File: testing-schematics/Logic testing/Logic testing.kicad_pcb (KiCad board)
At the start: 2 copper layers, 79 x 76.8 mm, 47 parts, among them IC1 ESP32-C6-WROOM-1U-N8, J1 External Box, J2 Aux Wire, J3 Conn_01x04, J4 Lame Tab, J5 Test Output, K1 G6K-2, K2 G6K-2, K3 G6K-2, K4 G6K-2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

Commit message: Work from 14th
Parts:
- added J6: Small Pin, Connector_Wire:SolderWire-0.5sqmm_1x01_D0.9mm_OD2.1mm, F.Cu at (117.2, 106.8)
- SW3: footprint Button_Switch_THT:SW_PUSH-12mm -> Button_Switch_THT:SW_PUSH_6mm_H13mm
- moved SW3 99.1 mm to (136.5, 111.8), turned to 180 degrees
- moved R9 66.4 mm to (91.5, 60.5)
- moved R11 53.3 mm to (124.0, 53.5), turned to 90 degrees
- moved C3 52.3 mm to (128.2, 53.5), turned to 90 degrees
- moved R5 52.1 mm to (94.2, 92.1)
- moved R7 50.3 mm to (94.2, 97.0)
- moved R4 48.2 mm to (94.2, 87.2), turned to 180 degrees
- moved R6 41.8 mm to (103.5, 94.4)
- moved R3 40.5 mm to (103.5, 90.6), turned to 180 degrees
- moved R2 39.3 mm to (103.5, 86.8), turned to 180 degrees
- moved R12 32.2 mm to (110.2, 90.6)
- moved R1 31.4 mm to (103.5, 98.2)
- moved R15 30.7 mm to (110.2, 86.8)
- moved R14 23.6 mm to (110.2, 94.4)
- moved R13 17.8 mm to (110.2, 98.2)
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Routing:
- net Net-(D4-A): track 0.00 -> 95.5 mm, vias 0 -> 3
- net Net-(D3-A): track 0.00 -> 80.5 mm
- net SG1: track 0.00 -> 66.6 mm, vias 0 -> 2
- net BTN USE: track 0.00 -> 63.7 mm, vias 0 -> 2
- net LAME: track 0.00 -> 57.2 mm, vias 0 -> 2
- net Net-(D1-A): track 0.00 -> 52.7 mm
- net Net-(P1-SHIELD): track 0.00 -> 52.3 mm, vias 0 -> 1
- net B2: track 0.00 -> 50.9 mm
- net VDR3: track 0.00 -> 50.0 mm, vias 0 -> 2
- net A1: track 0.00 -> 47.4 mm
- net Net-(Q1-B): track 0.00 -> 46.7 mm
- net Net-(Q2-B): track 0.00 -> 46.1 mm, vias 0 -> 1
- net Net-(D2-A): track 0.00 -> 44.5 mm
- net Net-(SW1-C): track 0.00 -> 40.9 mm, vias 0 -> 2
- net B1: track 0.00 -> 38.6 mm
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- added copper zone on B.Cu, net VD1
- added copper zone on F.Cu, net VD1
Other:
- board size 79 x 76.8 mm -> 79 x 78.2 mm

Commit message: Finished PCB
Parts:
- moved SW2 0.16 mm to (100.8, 49.6)
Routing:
- net WT2: track 27.8 -> 182.0 mm, vias 0 -> 9
- net +5V: track 27.4 -> 175.1 mm, vias 2 -> 8
- net C1: track 15.5 -> 79.7 mm, vias 0 -> 4
- net C2: track 15.5 -> 77.2 mm, vias 0 -> 3
- net A2: track 36.4 -> 93.1 mm, vias 0 -> 2
- net Net-(Q4-B): track 0.00 -> 48.6 mm, vias 0 -> 3
- net VDR2: track 20.7 -> 58.9 mm, vias 0 -> 2
- net WT1: track 0.00 -> 36.6 mm, vias 0 -> 2
- net WPS A: track 28.6 -> 59.3 mm, vias 2 -> 4
- net WPS B: track 26.6 -> 56.9 mm, vias 2 -> 3
- net VDR1: track 29.9 -> 54.1 mm, vias 0 -> 2
- net WT3: track 0.00 -> 20.7 mm, vias 0 -> 2
- net VD1: track 18.1 -> 31.0 mm, vias 2 -> 38
- net Net-(JP1-A): track 0.00 -> 9.68 mm
- net Net-(P1-SHIELD): track 52.3 -> 58.2 mm, vias 1 -> 0
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
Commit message: Finished PCB; Updated USB-C connector; Stated on CAD
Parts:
- added H5: MountingHole, MountingHole:MountingHole_2.2mm_M2_DIN965_Pad_TopBottom, F.Cu at (115.2, 58.8)
- added H6: MountingHole, MountingHole:MountingHole_2.2mm_M2_DIN965_Pad_TopBottom, F.Cu at (86.2, 58.8)
- added H7: MountingHole, MountingHole:MountingHole_2.2mm_M2_DIN965_Pad_TopBottom, F.Cu at (115.2, 100.8)
- added H8: MountingHole, MountingHole:MountingHole_2.2mm_M2_DIN965_Pad_TopBottom, F.Cu at (86.2, 100.8)
- P1: footprint Connector_USB:USB_C_Receptacle_GCT_USB4105-xx-A_16P_TopMnt_Horizontal -> Connector_USB:USB_C_Receptacle_GCT_USB4085
- moved P1 3.57 mm to (91.9, 53.4)
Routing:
- net VD1: track 31.0 -> 19.3 mm, vias 38 -> 40
- net Net-(P1-SHIELD): track 58.2 -> 53.2 mm, vias 0 -> 1
- net +5V: track 175.1 -> 178.7 mm, vias 8 -> 7
- net USB_D-: track 27.4 -> 30.6 mm, vias 2 -> 1
- net USB_D+: track 28.5 -> 30.9 mm, vias 2 -> 1
- net Net-(P1-CC): track 6.20 -> 8.10 mm
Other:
- outline, holes or cut-outs redrawn
- board text added: "FencingTester V1.0.0"
- board text added: "JLCJLCJLCJLC"
- board text added: "JoshLambda | Highway 2025"

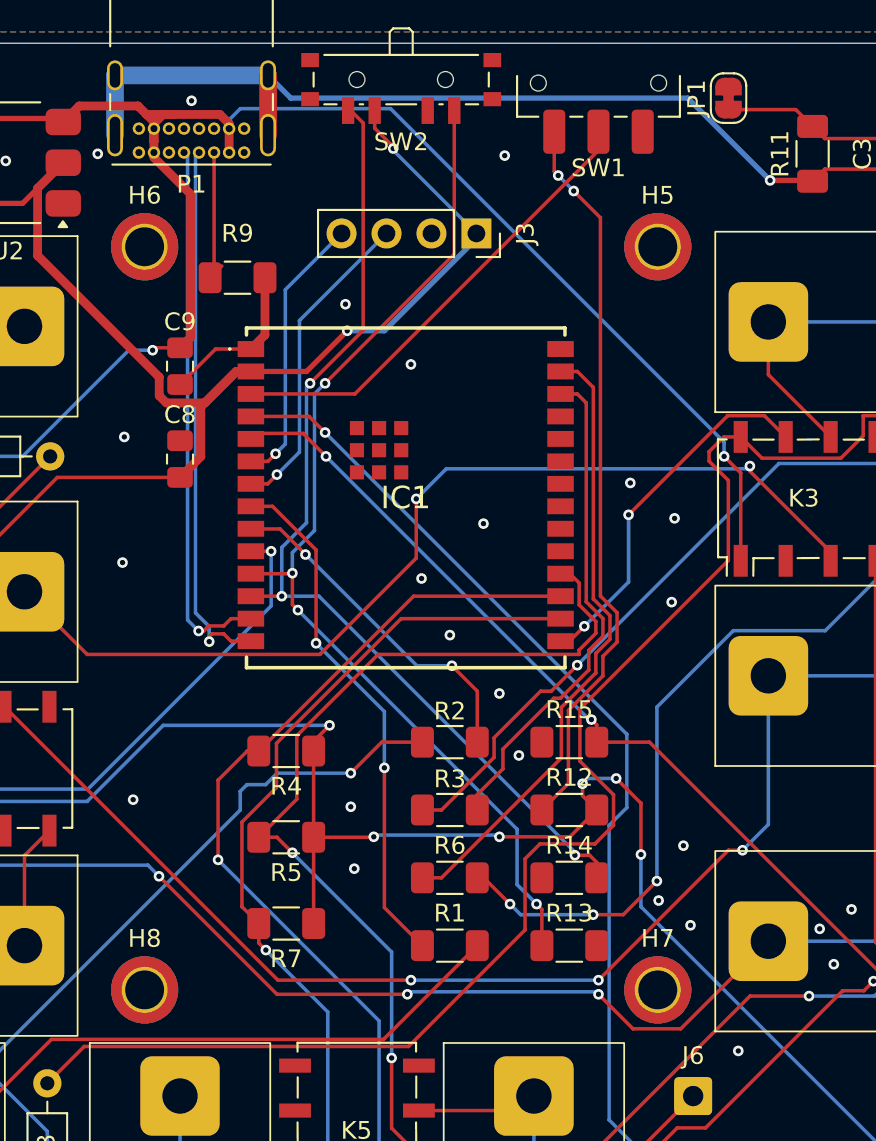
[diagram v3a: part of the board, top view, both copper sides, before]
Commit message: More final changes to PCB; Added cut outs & 3mm to CAD; Started programming
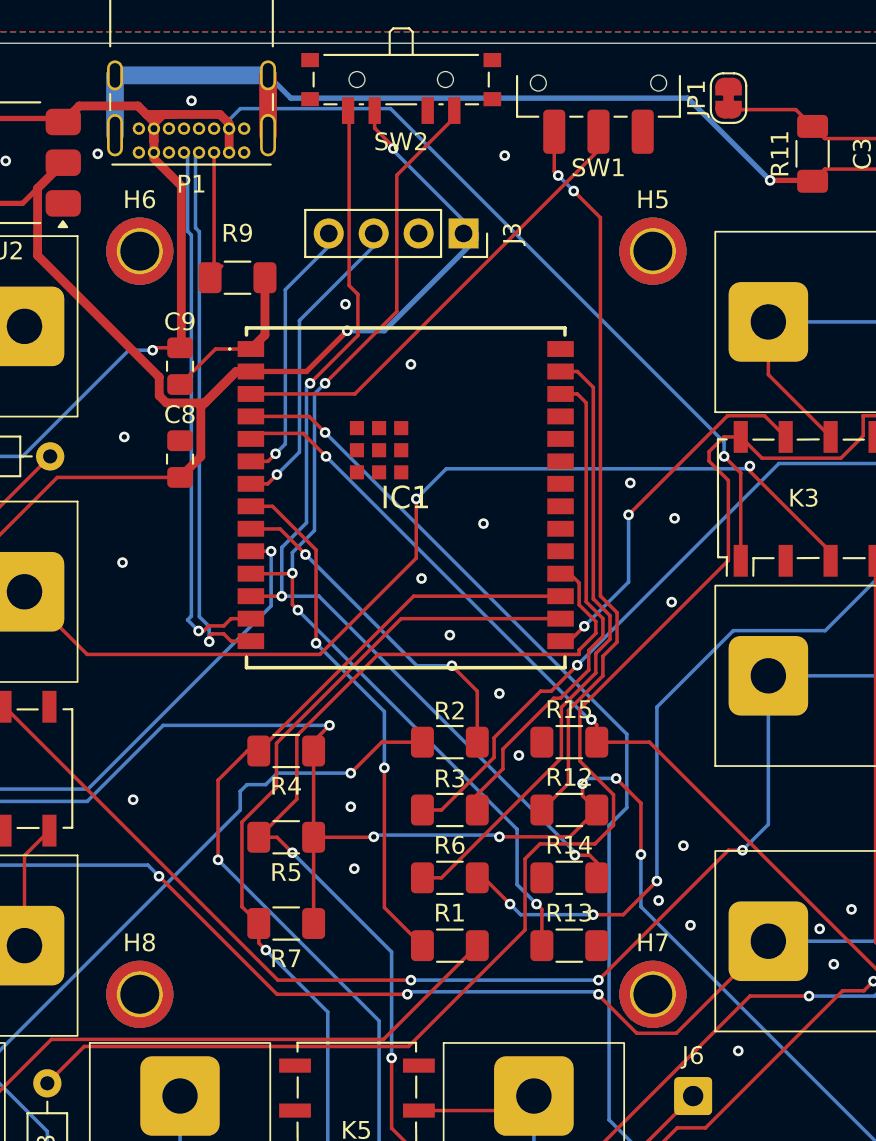
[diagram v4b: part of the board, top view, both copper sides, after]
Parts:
- moved J3 0.72 mm to (104.3, 58.0)
- moved H5 0.37 mm to (115.0, 59.0)
- moved H6 0.37 mm to (86.0, 59.0)
- moved H7 0.37 mm to (115.0, 101.0)
- moved H8 0.37 mm to (86.0, 101.0)

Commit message: Worked on  issues
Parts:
- added D5: 1N4148, Diode_SMD:D_SOD-123, F.Cu at (127.0, 89.4)
- added K6: G6K-2, Relay_SMD:Relay_DPDT_Omron_G6K-2F, F.Cu at (134.5, 73.0)
- added Q5: BC547, Package_TO_SOT_THT:TO-92_Inline, F.Cu at (123.0, 90.1)
- added R16: 10k, Custom:R_1206_3216Metric_Pad1.30x1.75mm_HandSolder_Text, F.Cu at (115.2, 73.1)
- added R17: 10k, Custom:R_1206_3216Metric_Pad1.30x1.75mm_HandSolder_Text, F.Cu at (85.3, 88.4)
- added R8: 510, Custom:R_1206_3216Metric_Pad1.30x1.75mm_HandSolder_Text, F.Cu at (116.2, 86.9)
- C3: footprint Capacitor_SMD:C_0603_1608Metric_Pad1.08x0.95mm_HandSolder -> Capacitor_SMD:C_0805_2012Metric_Pad1.18x1.45mm_HandSolder
- D1, D2, D3, D4: footprint Diode_THT:D_DO-35_SOD27_P7.62mm_Horizontal -> Diode_SMD:D_SOD-123
- R1, R11, R12, R13, R14, R15, R2, R3, R4, R5, R6, R7, R9: footprint Resistor_SMD:R_1206_3216Metric_Pad1.30x1.75mm_HandSolder -> Custom:R_1206_3216Metric_Pad1.30x1.75mm_HandSolder_Text
- moved Q4 76.2 mm to (80.3, 121.2)
- moved D3 55.7 mm to (131.8, 91.6), turned to 0 degrees
- moved Q1 43.4 mm to (78.2, 71.1), turned to 0 degrees
- moved Q2 37.5 mm to (65.2, 70.4), turned to 180 degrees
- moved R12 36.8 mm to (121.0, 55.4)
- moved R1 27.6 mm to (87.2, 76.0), turned to -90 degrees
- moved R6 27.3 mm to (80.8, 109.5), turned to -90 degrees
- moved R2 22.1 mm to (84.2, 76.0), turned to -90 degrees
- moved Q3 21.5 mm to (135.7, 90.9), turned to 0 degrees
- moved R5 19.1 mm to (112.7, 86.9), turned to 90 degrees
- moved R7 17.1 mm to (108.0, 86.9), turned to 90 degrees
- moved R4 16.1 mm to (110.3, 86.9), turned to 90 degrees
- moved R13 14.5 mm to (101.2, 86.9), turned to -90 degrees
- moved R14 13.6 mm to (99.0, 86.9), turned to 90 degrees
- moved R3 11.4 mm to (114.5, 93.2), turned to 0 degrees
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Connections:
- IC1 pad 10: WT1 -> VD1
- IC1 pad 15: WT3 -> VD1
- K4 pad 4: SG1 -> Net-(K4-Pad4)
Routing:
- net Net-(D4-A): track 95.5 -> 28.1 mm, vias 3 -> 0
- net Net-(K4-Pad4): track 0.00 -> 67.4 mm, vias 0 -> 2
- net SG1: track 66.6 -> 11.7 mm, vias 2 -> 0
- net +5V: track 178.3 -> 232.7 mm, vias 7 -> 9
- net Net-(D3-A): track 82.7 -> 30.9 mm, vias 0 -> 2
- net Net-(Q1-B): track 46.7 -> 10.8 mm
- net Net-(Q4-B): track 48.6 -> 12.8 mm, vias 3 -> 0
- net Net-(SW1-C): track 41.6 -> 12.8 mm, vias 2 -> 0
- net Net-(D1-A): track 52.7 -> 26.5 mm, vias 0 -> 1
- net Net-(D5-A): track 0.00 -> 24.8 mm
- net Net-(D2-A): track 44.5 -> 20.3 mm, vias 0 -> 1
- net REL1: track 29.6 -> 5.43 mm, vias 2 -> 0
- net Net-(Q2-B): track 46.7 -> 23.6 mm, vias 1 -> 0
- net REL4: track 35.4 -> 56.3 mm, vias 0 -> 2
- net WPS B: track 56.5 -> 40.4 mm, vias 3 -> 2
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
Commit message: Worked on PCB; worked on Code; Worked on journal
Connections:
- IC1 pad 19: unconnected-(IC1-IO21-Pad19) -> REL5
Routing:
- net REL5: track 0.00 -> 12.6 mm, vias 0 -> 2
- net VD1: vias 33 -> 57
- net C1: vias 4 -> 3
- net (no net): vias 0 -> 1
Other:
- board text added: "A1"
- board text added: "A2"
- board text added: "A3"
- board text added: "B1"
- board text added: "B2"
- board text added: "B3"
- board text added: "C1"
- board text added: "C2"
- board text added: "C3"
- board text added: "LAME"
- board text added: "OLED"
- board text added: "PWR"
- board text added: "WEAPON"

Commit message: Made last changes to CAD, PCB, & journal. Ready for submission
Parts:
- K1, K2, K3, K4, K5, K6: footprint Relay_SMD:Relay_DPDT_Omron_G6K-2F -> Relay_SMD:Relay_DPDT_Omron_G6K-2F-Y
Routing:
- net A2: track 93.1 -> 94.7 mm
- net +5V: track 233.1 -> 231.7 mm
- net VDR1: track 46.3 -> 47.0 mm
- net WT1: track 20.6 -> 21.2 mm
- net WT3: track 8.31 -> 8.85 mm
- net WT2: track 192.1 -> 191.6 mm
